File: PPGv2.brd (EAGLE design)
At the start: 56.8 x 49.5 mm, 54 parts

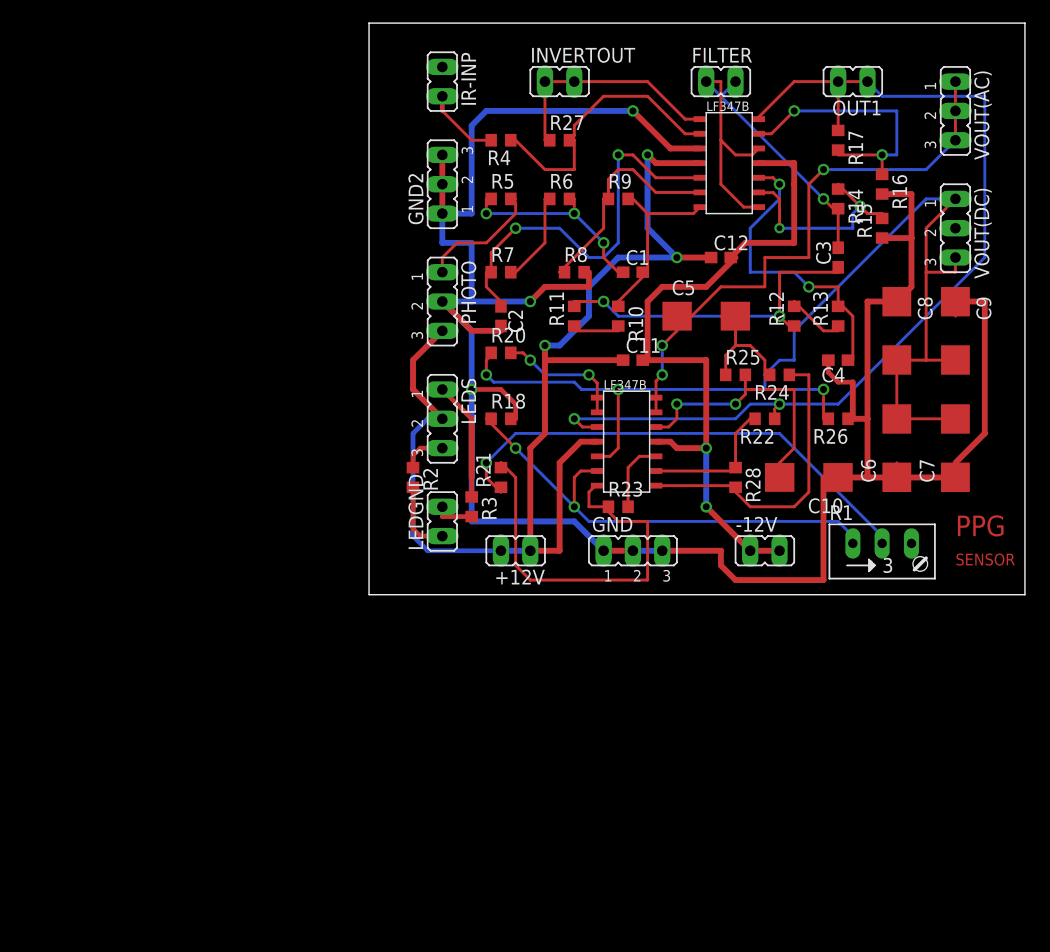
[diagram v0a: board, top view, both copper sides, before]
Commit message: Final
-made 2 layers each with one IC
-final dimensions are 46.15 x 35.8 mm acc to OSHpark guidelines
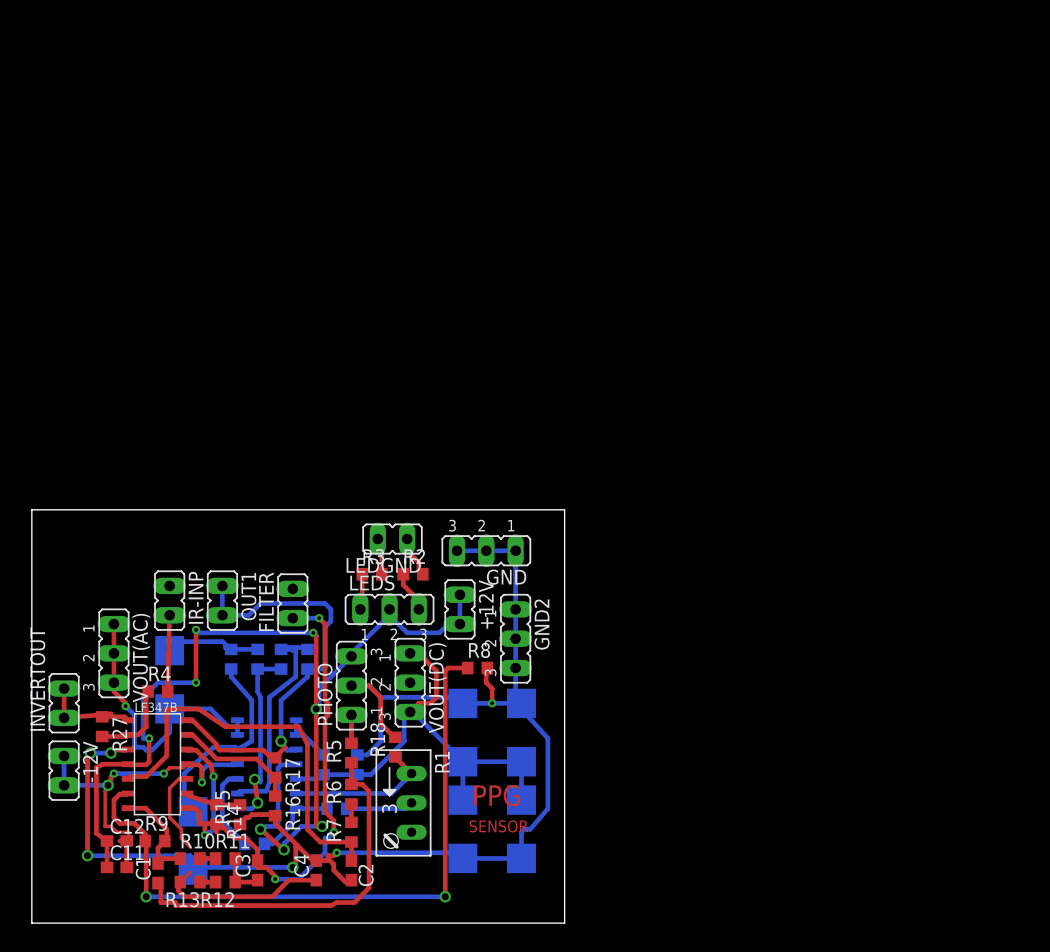
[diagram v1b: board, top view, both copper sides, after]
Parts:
- moved VOUT(AC) 86.7 mm to (-22.1, -1.27)
- moved R14 75.8 mm to (-13.2, -15.2)
- moved R15 75.3 mm to (-11.2, -15.2)
- moved R16 75.3 mm to (-8.13, -14.5)
- moved R13 74.5 mm to (-15.5, -21.1), turned to 180 degrees
- moved C3 73.1 mm to (-9.65, -20.1)
- moved R17 73.0 mm to (-8.13, -11.2)
- moved C12 72.8 mm to (-21.8, -17.5)
- moved U$1 71.9 mm to (-20.3, -15.2)
- moved OUT1 70.7 mm to (-12.7, 3.30), turned to 180 degrees
- moved R12 69.5 mm to (-12.4, -21.1), turned to 180 degrees
- moved INVERTOUT 68.9 mm to (-26.4, -5.59), turned to 0 degrees
- moved R9 68.6 mm to (-18.5, -17.5)
- moved C1 66.4 mm to (-18.3, -20.3), turned to 90 degrees
- moved R27 64.4 mm to (-23.1, -7.62), turned to 270 degrees
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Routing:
- net GND: track 211.6 -> 130.5 mm, vias 3 -> 6
- net N$29: track 101.7 -> 39.9 mm, vias 3 -> 0
- net N$22: track 84.8 -> 38.9 mm, vias 2 -> 1
- net N$10: track 19.5 -> 59.3 mm, vias 0 -> 2
- net N$25: track 43.1 -> 5.84 mm, vias 1 -> 0
- net -12V: track 61.4 -> 31.6 mm, vias 2 -> 4
- net N$26: track 41.8 -> 12.7 mm, vias 2 -> 0
- net N$24: track 34.9 -> 7.32 mm
- net N$14: track 30.3 -> 4.04 mm, vias 2 -> 0
- net N$20: track 49.8 -> 25.0 mm, vias 3 -> 1
- net N$4: track 24.2 -> 7.28 mm
- net N$6: track 18.1 -> 32.8 mm, vias 3 -> 0
- net N$16: track 18.8 -> 4.81 mm, vias 2 -> 0
- net N$19: track 23.8 -> 10.8 mm, vias 2 -> 0
- net N$18: track 39.6 -> 52.2 mm, vias 1 -> 5
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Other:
- board size 56.8 x 49.5 mm -> 46.2 x 35.8 mm

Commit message: Before removing the extra Pins
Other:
- board size 46.2 x 35.8 mm -> 45.9 x 35.8 mm
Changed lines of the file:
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@@
 <board>
 <plain>
-<wire x1="-29.21" y1="-24.638" x2="16.942" y2="-24.638" width="0" layer="20"/>
-<wire x1="16.942" y1="-24.638" x2="16.942" y2="11.166" width="0" layer="20"/>
-<wire x1="16.942" y1="11.166" x2="-29.21" y2="11.166" width="0" layer="20"/>
+<wire x1="-29.21" y1="-24.638" x2="16.688" y2="-24.638" width="0" layer="20"/>
+<wire x1="16.688" y1="-24.638" x2="16.688" y2="11.166" width="0" layer="20"/>
+<wire x1="16.688" y1="11.166" x2="-29.21" y2="11.166" width="0" layer="20"/>
 <wire x1="-29.21" y1="11.166" x2="-29.21" y2="-24.638" width="0" layer="20"/>
 <text x="8.89" y="-14.478" size="1.778" layer="1" font="vector">PPG</text>

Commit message: Final
-removed extra connectors
-without IR-INP input
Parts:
- removed +12V, -12V, FILTER, INVERTOUT, IR-INP, LEDGND, OUT1: (no value), jumper:JP1
- removed GND, GND2, LEDS, VOUT(DC): (no value), jumper:JP2
- removed R2, R27, R3, R4: (no value), resistor:R0603
- moved C10 23.8 mm to (4.06, -3.56), flipped to the top
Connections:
- removed net N$2 (its old number): IR-INP.2, R4.2
- removed net N$28: LEDS.3, R2.1
- removed net N$3: LEDS.1, R3.1
- removed net N$30: LEDGND.2, R3.2
- removed net N$33: LEDGND.1, R2.2
- removed net N$4: R27.2, R4.1, U$1.P$2
- removed net N$5: INVERTOUT.1, INVERTOUT.2, R27.1, U$1.P$1
- net +12V: now also VOUT(AC).2; no longer +12V.1, +12V.2, LEDS.2
- net -12V: now also VOUT(AC).3; no longer -12V.1, -12V.2
- net GND: no longer GND.1, GND.2, GND.3, GND2.1, GND2.2, GND2.3, U$1.P$3
- net N$18: no longer FILTER.1, FILTER.2
- net N$20: no longer VOUT(AC).2, VOUT(AC).3
- net N$22: no longer OUT1.1, OUT1.2
- net N$29: no longer VOUT(DC).1, VOUT(DC).3
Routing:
- net GND: track 130.5 -> 90.3 mm, vias 6 -> 1
- net N$18: track 52.2 -> 20.1 mm, vias 5 -> 2
- net +12V: track 93.8 -> 73.5 mm, vias 8 -> 4
- net N$22: track 38.9 -> 21.7 mm
- net N$32: track 17.5 -> 31.7 mm, vias 0 -> 1
- net N$29: track 39.9 -> 28.2 mm
- net N$11: track 22.4 -> 32.4 mm, vias 0 -> 2
- net N$5: track 9.34 -> 0.00 mm
- net N$4: track 7.28 -> 0.00 mm
- net N$2 (its old number): track 6.61 -> 0.00 mm
- net N$20: track 25.0 -> 18.8 mm
- net N$27: track 4.36 -> 9.82 mm, vias 0 -> 2
- net N$28: track 3.82 -> 0.00 mm
- net N$33: track 3.61 -> 0.00 mm
- net N$30: track 3.19 -> 0.00 mm
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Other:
- board size 45.9 x 35.8 mm -> 42.1 x 36.3 mm
- board text removed: "PPG"
- board text removed: "SENSOR"

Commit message: -final
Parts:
- moved PHOTO 2.09 mm to (-1.02, -2.03), turned to 270 degrees
- moved C4 1.02 mm to (-5.59, -20.1)
- turned VOUT(AC) to 90 degrees
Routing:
- net N$1: track 2.45 -> 12.8 mm, vias 0 -> 1
- net -12V: track 31.6 -> 41.5 mm, vias 2 -> 5
- net N$20: track 18.8 -> 14.6 mm
- net N$18: track 20.1 -> 22.4 mm
- net GND: track 90.3 -> 92.0 mm, vias 1 -> 2
- net N$13: track 0.00 -> 1.35 mm
- net N$11: track 32.4 -> 31.4 mm
- net +12V: track 73.5 -> 72.7 mm
- net N$32: track 31.7 -> 32.5 mm
- added copper zone on layer 1, net GND
- added copper zone on layer 16, net GND
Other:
- board size 42.1 x 36.3 mm -> 42.1 x 28.7 mm

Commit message: -minor changes
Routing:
- net -12V: track 41.5 -> 40.2 mm, vias 5 -> 4
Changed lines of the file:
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@@
 <element name="U$1" library="Op+Amps" package="SOIC14" value="LF347-14SOIC" x="-20.32" y="-15.24" smashed="yes"/>
 <element name="U$2" library="Op+Amps" package="SOIC14" value="LF347-14SOIC" x="-6.858" y="-15.24" smashed="yes" rot="MR0"/>
-<element name="R5" library="resistor" package="R0603" value="" x="-1.524" y="-9.906" rot="R90"/>
+<element name="R5" library="resistor" package="R0603" value="" x="-1.524" y="-9.906" smashed="yes" rot="R90">
+<attribute name="NAME" x="-1.905" y="-9.525" size="1.27" layer="25" rot="R90"/>
+<attribute name="VALUE" x="0.508" y="-10.795" size="1.27" layer="27" rot="R90"/>
+</element>
 <element name="R6" library="resistor" package="R0603" value="" x="-1.524" y="-13.462" rot="R90"/>
 <element name="R7" library="resistor" package="R0603" value="" x="-1.524" y="-16.764" rot="R90"/>
@@
 <element name="R17" library="resistor" package="R0603" value="" x="-8.128" y="-11.176" rot="R270"/>
 <element name="R18" library="resistor" package="R0603" value="" x="2.286" y="-9.398" rot="R90"/>
-<element name="R20" library="resistor" package="R0603" value="" x="-3.937" y="-10.922" rot="MR90"/>
+<element name="R20" library="resistor" package="R0603" value="" x="-3.937" y="-10.922" smashed="yes" rot="MR90">
+<attribute name="NAME" x="-5.842" y="-12.065" size="1.27" layer="26" rot="MR90"/>
+<attribute name="VALUE" x="-5.969" y="-11.811" size="1.27" layer="28" rot="MR90"/>
+</element>
 <element name="R21" library="resistor" package="R0603" value="" x="-2.794" y="-14.732" rot="MR0"/>
 <element name="R22" library="resistor" package="R0603" value="" x="-5.334" y="-1.778" rot="MR90"/>
@@
 <element name="R24" library="resistor" package="R0603" value="" x="-9.652" y="-1.778" rot="MR90"/>
 <element name="R25" library="resistor" package="R0603" value="" x="-11.938" y="-1.778" rot="MR270"/>
-<element name="R26" library="resistor" package="R0603" value="" x="-1.016" y="-10.922" rot="MR270"/>
+<element name="R26" library="resistor" package="R0603" value="" x="-1.016" y="-10.922" smashed="yes" rot="MR270">
+<attribute name="NAME" x="-1.651" y="-9.017" size="1.27" layer="26" rot="MR270"/>
+<attribute name="VALUE" x="1.016" y="-10.033" size="1.27" layer="28" rot="MR270"/>
+</element>
 <element name="C1" library="CEDTv69" package="C0603" value="" x="-18.288" y="-20.32" rot="R90"/>
 <element name="C2" library="CEDTv69" package="C0603" value="" x="-1.524" y="-20.066" rot="R270"/>
@@
 <wire x1="-1.524" y1="-17.614" x2="-4.23" y2="-17.614" width="0.4064" layer="1"/>
 <wire x1="-4.23" y1="-17.614" x2="-5.334" y2="-16.51" width="0.4064" layer="1"/>
-<wire x1="-5.334" y1="-16.51" x2="-5.334" y2="-9.144" width="0.4064" layer="1"/>
-<wire x1="-5.334" y1="-9.144" x2="-6.096" y2="-7.62" width="0.4064" layer="1"/>
+<wire x1="-5.334" y1="-16.51" x2="-5.334" y2="-9.398" width="0.4064" layer="1"/>
+<wire x1="-5.334" y1="-9.398" x2="-6.096" y2="-7.62" width="0.4064" layer="1"/>
 <wire x1="-6.096" y1="-7.62" x2="-12.446" y2="-7.62" width="0.4064" layer="1"/>
 <wire x1="-12.446" y1="-7.62" x2="-14.732" y2="-6.096" width="0.4064" layer="1"/>
@@
 <wire x1="-18.542" y1="-9.652" x2="-17.78" y2="-9.652" width="0.4064" layer="16"/>
 <wire x1="-18.288" y1="-9.398" x2="-18.542" y2="-9.652" width="0.4064" layer="1"/>
-<wire x1="-18.288" y1="1.27" x2="-18.288" y2="-9.398" width="0.4064" layer="1"/>
-<wire x1="-22.098" y1="1.27" x2="-18.288" y2="1.27" width="0.4064" layer="16"/>
 <via x="-18.542" y="-9.652" extent="1-16" drill="0.6"/>
-<via x="-18.288" y="1.27" extent="1-16" drill="0.6"/>
+<wire x1="-18.288" y1="-9.398" x2="-18.542" y2="-9.144" width="0.4064" layer="1"/>
+<wire x1="-18.542" y1="-9.144" x2="-18.542" y2="-0.762" width="0.4064" layer="1"/>
+<wire x1="-18.542" y1="-0.762" x2="-20.574" y2="1.27" width="0.4064" layer="1"/>
+<wire x1="-20.574" y1="1.27" x2="-22.098" y2="1.27" width="0.4064" layer="1"/>
 </signal>
 <signal name="+12V">
